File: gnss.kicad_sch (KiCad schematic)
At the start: 72 parts, among them J11 SMA-KE-347-H13.5-1.6, J12 U.FL, Q12 AO3401A, Q13 BSS138, SW4 RESET_GNSS, SW5 SAFEBOOT_GNSS, U10 TPS7A2033PDBVR, U11 TPS259474LRPWR, U9 NEO-F10N

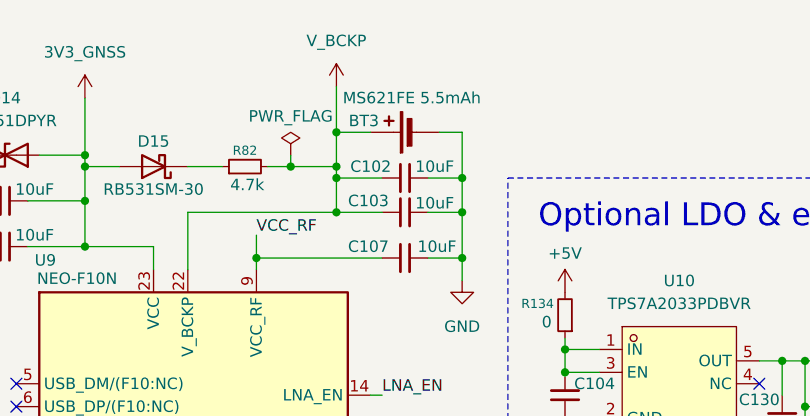
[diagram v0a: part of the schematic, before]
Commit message: Add silkscreen graphics
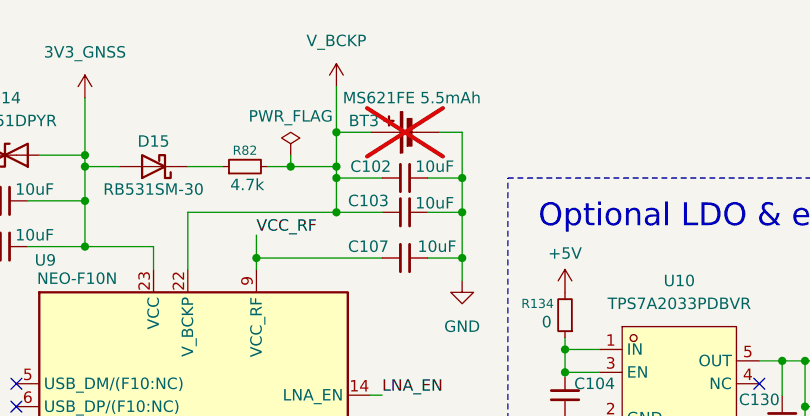
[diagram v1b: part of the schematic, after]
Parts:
- BT3: now not fitted
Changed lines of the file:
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@@
 		(on_board yes)
 		(in_pos_files yes)
-		(dnp no)
+		(dnp yes)
 		(property "Reference" "BT3"
 			(at 142.748 25.4 90)
